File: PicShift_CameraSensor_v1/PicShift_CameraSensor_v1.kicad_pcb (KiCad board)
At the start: 2 copper layers, 55.9 x 32 mm, 72 parts, among them J1 Conn_01x11, J2 Conn_01x11, U1 ADG732BSUZ, U2 ADG732BSUZ

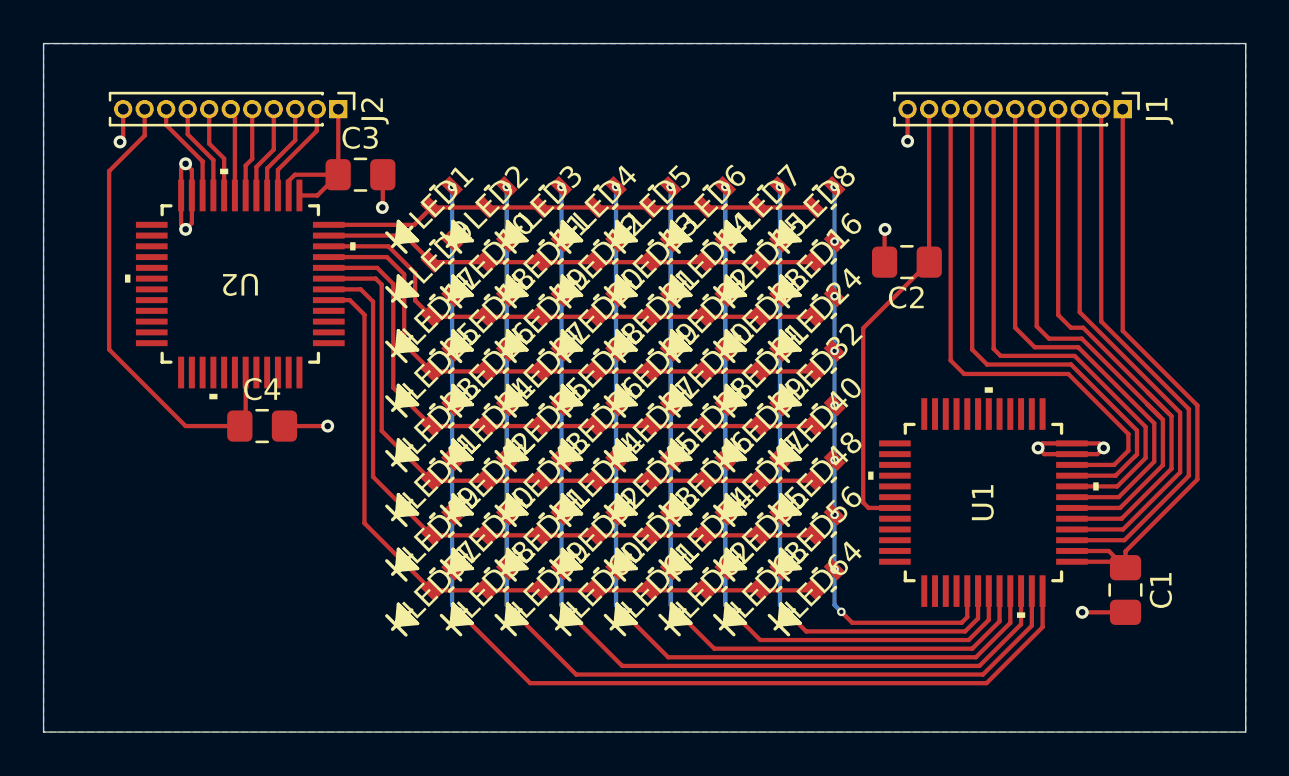
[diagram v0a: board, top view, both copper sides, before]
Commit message: Fixed all DRC for OSHPARK
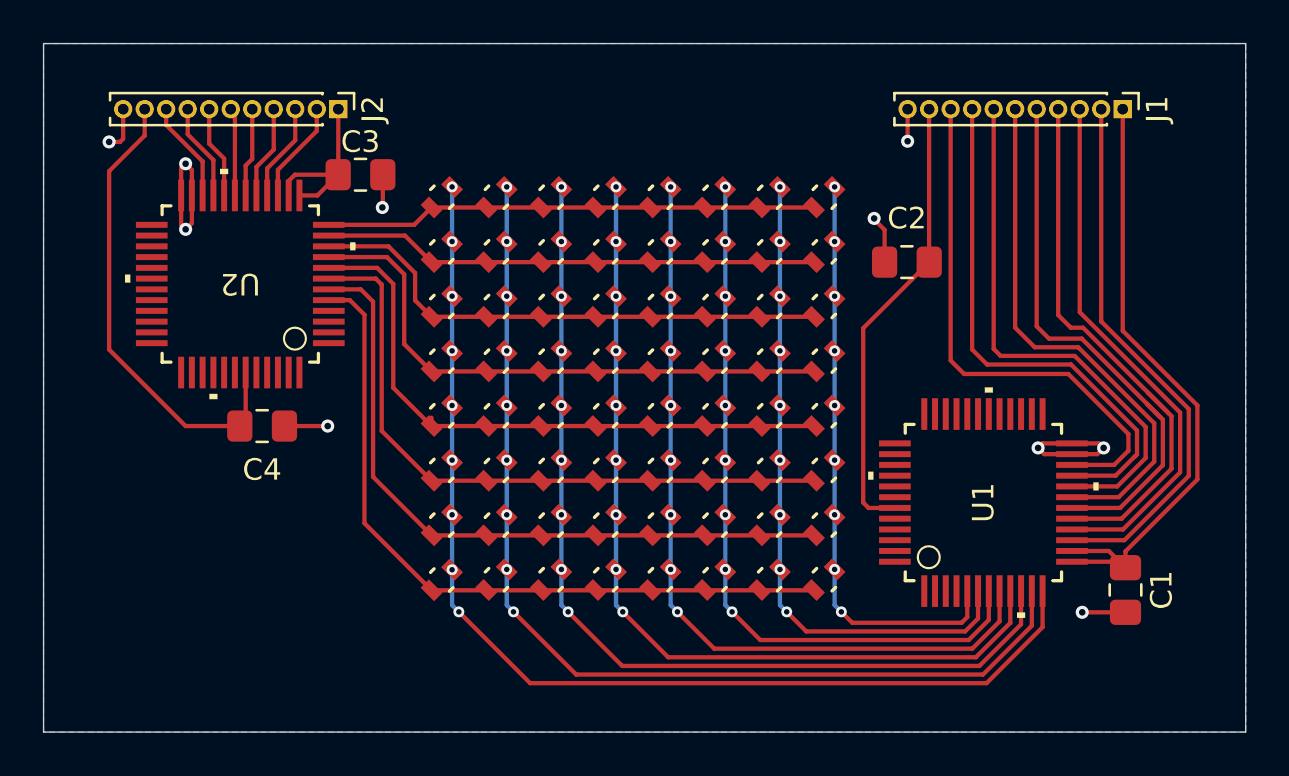
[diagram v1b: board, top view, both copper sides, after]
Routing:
- net GND: track 23.3 -> 24.5 mm
